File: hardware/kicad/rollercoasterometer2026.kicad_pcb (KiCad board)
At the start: 2 copper layers, 48.3 x 114.3 mm, 32 parts, among them J1 Micro_SD_Card, J102 Conn_02x07_Counter_Clockwise, J103 ZED-F9R U.FL, J104 LIS2MDL, J105 BMP595, J106 ADXL375, J4 SM03B-SRSS-TB, U101 RPiPico2, U102 ADIS16465-2BMLZ, U2 LIS2MDLTR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

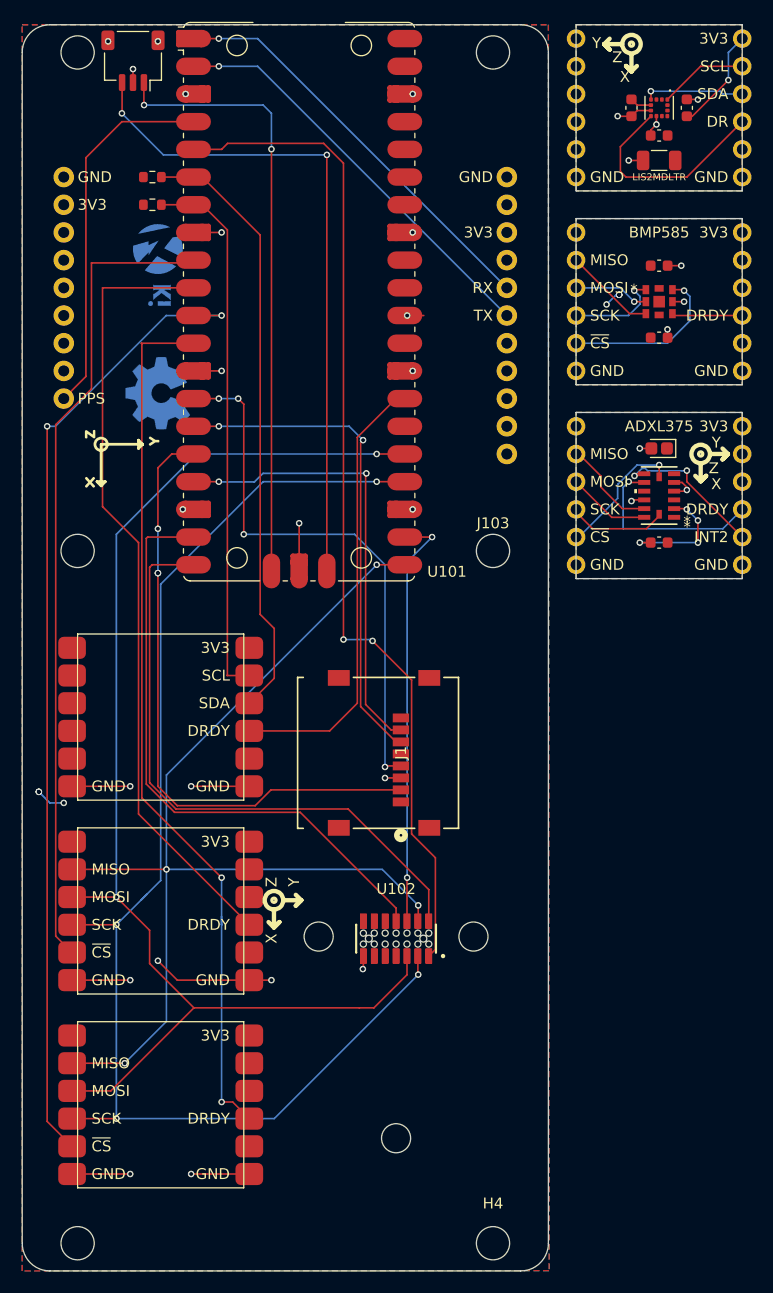
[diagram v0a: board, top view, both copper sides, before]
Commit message: Updated board to four layer design
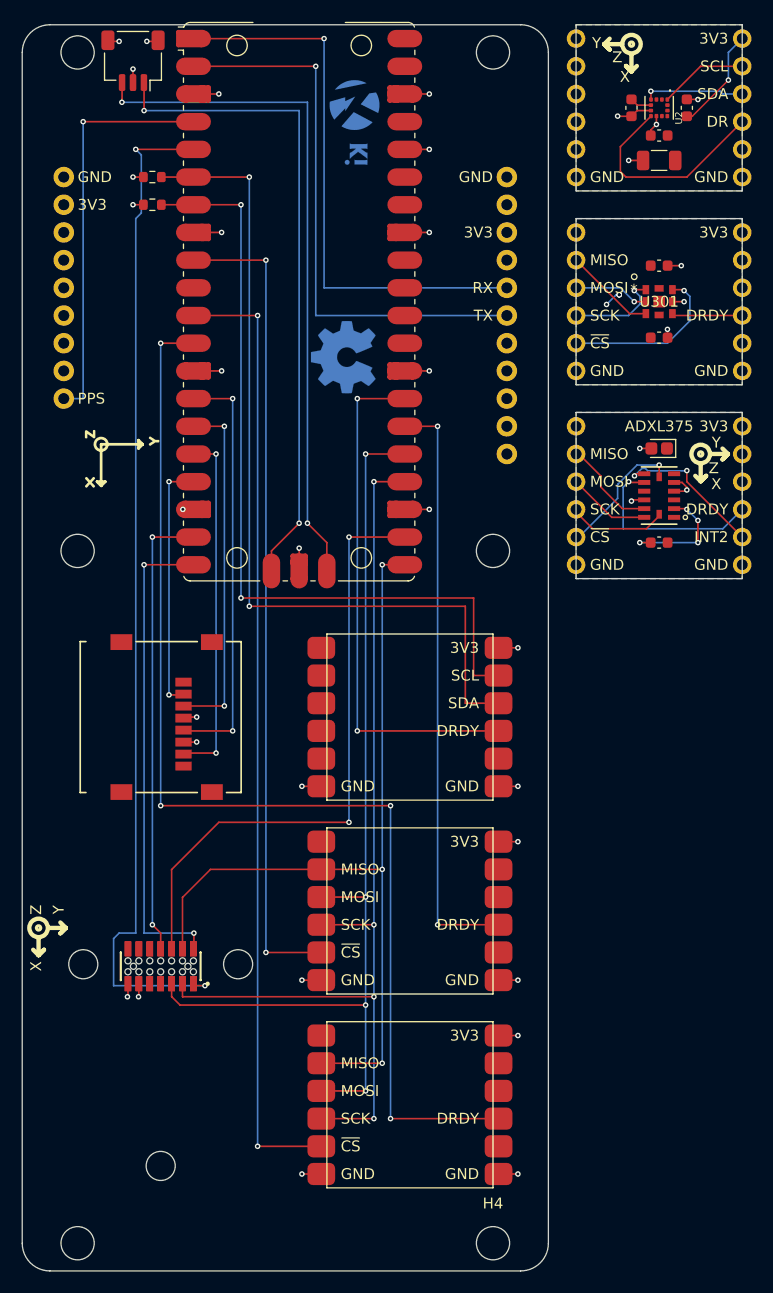
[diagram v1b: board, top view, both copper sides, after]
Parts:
- moved J104 22.9 mm to (109.2, 139.7)
- moved J105 22.9 mm to (109.2, 157.5)
- moved J106 22.9 mm to (109.2, 175.3)
- moved G103 22.4 mm to (104.1, 83.6)
- moved G102 22.2 mm to (104.4, 89.9)
- moved J102 21.7 mm to (86.4, 162.6)
- moved U102 21.7 mm to (86.4, 162.6)
- moved J101 20.2 mm to (86.4, 139.7)
- moved G101 17.3 mm to (103.1, 106.7)
- renumbered J1 to J101
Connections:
- U101 pad 10: /DR_BMP -> unconnected-(U101-GP7-Pad10)
- U101 pad 26: /~{CS}_MAG -> /DR_BMP
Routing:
- net /SCK0: track 119.9 -> 88.8 mm
- net /MOSI0: track 116.0 -> 88.6 mm, vias 2 -> 4
- net /MISO1: track 57.2 -> 31.7 mm, vias 3 -> 2
- net /SCL0: track 49.9 -> 74.1 mm, vias 0 -> 2
- net /DR_HIG: track 82.2 -> 105.9 mm, vias 2 -> 4
- net /SDA0: track 55.7 -> 79.2 mm, vias 0 -> 2
- net GND: track 58.7 -> 38.5 mm, vias 21 -> 20
- net /MISO0: track 96.5 -> 76.7 mm, vias 4 -> 3
- net /DR_BMP: track 73.1 -> 55.1 mm, vias 0 -> 2
- net /~{CS}_SD: track 41.0 -> 24.0 mm
- net /~{CS}_IMU: track 39.5 -> 55.8 mm
- net /~{RST}_IMU: track 56.5 -> 42.7 mm, vias 0 -> 2
- net /MOSI1: track 44.8 -> 31.4 mm
- net /TX_GPS: track 37.4 -> 50.8 mm
- net /RX_GPS: track 37.4 -> 50.8 mm
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- added copper zone on In2.Cu, net +3V3
- added copper zone on In1.Cu, net GND
- removed copper zone on F.Cu, net +3V3
- removed copper zone on B.Cu, net GND
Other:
- copper layers 2 -> 4
- rule pad_to_mask_clearance: 0.051 -> 0

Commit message: Moved sensors from stamp to direct placement
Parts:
- removed J104: LIS2MDL, footprints:StampPad
- removed J105: BMP595, footprints:StampPad
- removed J106: ADXL375, footprints:StampPad
- removed J201, J301, J401: ~, footprints:Stamp
- moved G302 63.4 mm to (113.3, 174.8)
- moved C406 60.6 mm to (109.2, 171.2)
- moved C208 60.4 mm to (109.2, 144.5)
- moved C209 60.4 mm to (109.2, 142.2)
- moved C304 60.4 mm to (109.2, 160.8)
- moved G301 60.4 mm to (106.7, 133.9)
- moved C210 60.4 mm to (111.8, 139.7)
- moved C308 60.4 mm to (109.2, 154.2)
- moved U2 60.4 mm to (109.2, 139.7)
- moved U301 60.4 mm to (109.2, 157.5)
- moved U401 60.4 mm to (109.2, 175.3)
- moved C205 60.4 mm to (106.7, 139.7)
- moved C401 59.9 mm to (109.2, 179.1)
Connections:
- C205 pad 2: /Magnetic Sensor/GND -> GND
- C208 pad 1: /Magnetic Sensor/3V3 -> +3V3
- C208 pad 2: /Magnetic Sensor/GND -> GND
- C209 pad 1: /Magnetic Sensor/3V3 -> +3V3
- C209 pad 2: /Magnetic Sensor/GND -> GND
- C210 pad 1: /Magnetic Sensor/3V3 -> +3V3
- C210 pad 2: /Magnetic Sensor/GND -> GND
- C304 pad 1: /Pressure Sensor/3V3 -> +3V3
- C304 pad 2: /Pressure Sensor/GND -> GND
- C308 pad 1: /Pressure Sensor/3V3 -> +3V3
- C308 pad 2: /Pressure Sensor/GND -> GND
- C401 pad 1: /HiG Sensor/3V3 -> +3V3
- C401 pad 2: /HiG Sensor/GND -> GND
- C406 pad 1: /HiG Sensor/3V3 -> +3V3
- C406 pad 2: /HiG Sensor/GND -> GND
- U2 pad 1: /Magnetic Sensor/SCL -> /SCL0
- U2 pad 10: /Magnetic Sensor/3V3 -> +3V3
- U2 pad 3: /Magnetic Sensor/3V3 -> +3V3
- U2 pad 4: /Magnetic Sensor/SDA -> /SDA0
- U2 pad 6: /Magnetic Sensor/GND -> GND
- U2 pad 7: /Magnetic Sensor/DRDY -> /DR_MAG
- U2 pad 8: /Magnetic Sensor/GND -> GND
- U2 pad 9: /Magnetic Sensor/3V3 -> +3V3
- U301 pad 1: /Pressure Sensor/SCK -> /SCK0
- U301 pad 2: /Pressure Sensor/MOSI -> /MOSI0
- U301 pad 3: /Pressure Sensor/MISO -> /MISO0
- U301 pad 4: /Pressure Sensor/3V3 -> +3V3
- U301 pad 5: /Pressure Sensor/DRDY -> /DR_BMP
- U301 pad 6: /Pressure Sensor/GND -> GND
- U301 pad 7: /Pressure Sensor/~{CS} -> /~{CS}_BMP
- U301 pad 8: /Pressure Sensor/3V3 -> +3V3
- U401 pad 1: /HiG Sensor/3V3 -> +3V3
- U401 pad 11: /HiG Sensor/GND -> GND
- U401 pad 12: /HiG Sensor/MISO -> /MISO0
- U401 pad 13: /HiG Sensor/MOSI -> /MOSI0
- U401 pad 14: /HiG Sensor/SCK -> /SCK0
- U401 pad 2: /HiG Sensor/GND -> GND
- U401 pad 3: /HiG Sensor/3V3 -> +3V3
- U401 pad 4: /HiG Sensor/GND -> GND
- U401 pad 5: /HiG Sensor/GND -> GND
- U401 pad 6: /HiG Sensor/3V3 -> +3V3
- U401 pad 7: /HiG Sensor/~{CS} -> /~{CS}_HIG
- U401 pad 9: /HiG Sensor/DRDY -> /DR_HIG
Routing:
- net /Magnetic Sensor/DRDY: track 19.6 -> 0.00 mm
- net /HiG Sensor/DRDY: track 17.5 -> 0.00 mm, vias 1 -> 0
- net /HiG Sensor/GND: track 16.1 -> 0.00 mm, vias 7 -> 0
- net /Pressure Sensor/~{CS}: track 15.0 -> 0.00 mm, vias 1 -> 0
- net +3V3: track 12.7 -> 27.1 mm, vias 8 -> 13
- net /HiG Sensor/INT2: track 14.2 -> 0.00 mm, vias 2 -> 0
- net /HiG Sensor/~{CS}: track 11.9 -> 0.00 mm, vias 1 -> 0
- net GND: track 38.5 -> 48.0 mm, vias 20 -> 25
- net /Magnetic Sensor/3V3: track 9.38 -> 0.00 mm, vias 1 -> 0
- net /HiG Sensor/SCK: track 8.99 -> 0.00 mm
- net /Magnetic Sensor/SDA: track 8.88 -> 0.00 mm, vias 1 -> 0
- net /HiG Sensor/MISO: track 8.61 -> 0.00 mm
- net /Pressure Sensor/SCK: track 8.48 -> 0.00 mm, vias 1 -> 0
- net /SDA0: track 79.2 -> 70.8 mm
- net /Pressure Sensor/MISO: track 8.28 -> 0.00 mm
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- removed copper zone on F.Cu, net /HiG Sensor/3V3
- removed copper zone on B.Cu, net /HiG Sensor/GND
- removed copper zone on F.Cu, net /Magnetic Sensor/3V3
- removed copper zone on B.Cu, net /Magnetic Sensor/GND
- removed copper zone on F.Cu, net /Pressure Sensor/3V3
- removed copper zone on B.Cu, net /Pressure Sensor/GND
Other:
- outline, holes or cut-outs redrawn

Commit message: Import rp2354 module
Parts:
- added C102: 10u, Capacitor_SMD:C_0805_2012Metric, F.Cu at (78.2, 87.4)
- added C103: 10u, Capacitor_SMD:C_0805_2012Metric, F.Cu at (89.4, 87.4)
- added C500: 10u, Capacitor_SMD:C_0805_2012Metric, F.Cu at (111.8, 188.0)
- added C501: 100n, Capacitor_SMD:C_0402_1005Metric, F.Cu at (77.3, 103.3)
- added C506: 100n, Capacitor_SMD:C_0402_1005Metric, F.Cu at (77.3, 105.7)
- added C511: 100n, Capacitor_SMD:C_0402_1005Metric, F.Cu at (77.3, 108.1)
- added C520: 100n, Capacitor_SMD:C_0402_1005Metric, F.Cu at (82.0, 112.8)
- added C521: 15p, Capacitor_SMD:C_0402_1005Metric, F.Cu at (82.4, 115.7)
- added C522: 15p, Capacitor_SMD:C_0402_1005Metric, F.Cu at (85.4, 115.7)
- added C523: 4.7u, Capacitor_SMD:C_0402_1005Metric, F.Cu at (84.6, 113.6)
- added C530: 100n, Capacitor_SMD:C_0402_1005Metric, F.Cu at (89.5, 110.7)
- added C538: 100n, Capacitor_SMD:C_0402_1005Metric, F.Cu at (90.9, 107.1)
- added C539: 100n, Capacitor_SMD:C_0402_1005Metric, F.Cu at (90.9, 106.1)
- added C544: 100n, Capacitor_SMD:C_0402_1005Metric, F.Cu at (90.3, 103.7)
- added C546: 4.7u, Capacitor_SMD:C_0402_1005Metric, F.Cu at (88.0, 101.6)
- added C549: 4.7u, footprints:C_0402_1005Metric_small_pads, F.Cu at (85.8, 102.1)
- added C550: 4.7u, footprints:C_0402_1005Metric_small_pads, F.Cu at (85.8, 101.1)
- added C553: 100n, Capacitor_SMD:C_0402_1005Metric, F.Cu at (81.7, 99.3)
- added H101: MountingHole, MountingHole:MountingHole_2.7mm_M2.5, F.Cu at (76.2, 78.7)
- added H102: MountingHole, MountingHole:MountingHole_2.7mm_M2.5, F.Cu at (119.9, 78.7)
- added J104: 2169900001, footprints:MOLEX_2169900001, F.Cu at (94.0, 76.2)
- added L550: 3.3u, footprints:L_pol_2016, F.Cu at (85.8, 99.5)
- added R101: 5.1k, Resistor_SMD:R_0402_1005Metric, F.Cu at (95.5, 85.9)
- added R102: 5.1k, Resistor_SMD:R_0402_1005Metric, F.Cu at (92.5, 85.9)
- added R522: 1k, Resistor_SMD:R_0402_1005Metric, F.Cu at (83.4, 113.6)
- added R526: 1k, Resistor_SMD:R_0402_1005Metric, F.Cu at (254.3, 89.4)
- added R546: 33, Resistor_SMD:R_0402_1005Metric, F.Cu at (88.0, 99.8)
- added R551: 27, Resistor_SMD:R_0402_1005Metric, F.Cu at (83.7, 99.3)
- added R552: 27, Resistor_SMD:R_0402_1005Metric, F.Cu at (82.7, 99.3)
- added R560: 1k, Resistor_SMD:R_0402_1005Metric, F.Cu at (77.2, 100.8)
- added S526: SW_Push, Button_Switch_SMD:SW_SPST_B3U-1000P, F.Cu at (68.8, 114.4)
- added S560: SW_Push, Button_Switch_SMD:SW_Push_1P1T_NO_Vertical_Wuerth_434133025816, F.Cu at (68.6, 121.6)
- added U501: RP2354A, footprints:RP2350-QFN-60-1EP_7x7_P0.4mm_EP3.4x3.4mm_ThermalVias, F.Cu at (83.8, 106.7)
- added Y501: ABM8-272-T3, Crystal:Crystal_SMD_3225-4Pin_3.2x2.5mm, F.Cu at (83.8, 119.1)
- R106, R107: footprint Resistor_SMD:R_0603_1608Metric -> Resistor_SMD:R_0402_1005Metric
- U101: value RPiPico2 -> NCP1117-3.3_SOT223; footprint footprints:RaspberryPi_Pico_Original_SMD -> Package_TO_SOT_SMD:SOT-223-3_TabPin2
- moved J103 57.2 mm to (119.4, 69.8)
- moved R106 52.6 mm to (109.2, 137.2), turned to 180 degrees
- moved R107 49.2 mm to (109.2, 135.9)
- moved G102 42.4 mm to (62.7, 98.0)
- moved G101 40.4 mm to (62.7, 108.5)
- moved G103 22.7 mm to (126.7, 85.1)
- moved U101 19.8 mm to (83.8, 88.9), turned to 180 degrees
- moved J101 9.77 mm to (82.3, 130.8)
- moved H103 2.54 mm to (76.2, 188.0)
- moved H104 2.54 mm to (119.4, 188.0)
- renumbered H3 to H103, H4 to H104, J4 to J105
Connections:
- U101 pad 1: /RX_GPS -> GND
- U101 pad 2: /TX_GPS -> +3V3
- U101 pad 3: GND -> VBUS
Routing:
- net /DR_HIG: track 108.2 -> 0.00 mm, vias 4 -> 0
- net /DR_IMU: track 94.5 -> 0.00 mm, vias 2 -> 0
- net /~{CS}_HIG: track 89.3 -> 0.00 mm, vias 2 -> 0
- net /MOSI0: track 89.4 -> 2.41 mm, vias 4 -> 1
- net /SCK0: track 86.3 -> 5.06 mm, vias 4 -> 1
- net /~{CS}_BMP: track 78.9 -> 0.00 mm, vias 2 -> 0
- net /MISO0: track 78.7 -> 7.08 mm, vias 4 -> 1
- net /SDA0: track 70.8 -> 0.00 mm, vias 2 -> 0
- net /SCL0: track 69.8 -> 0.00 mm, vias 2 -> 0
- net /SWD: track 61.5 -> 3.55 mm, vias 2 -> 1
- net /SWCLK: track 59.3 -> 1.85 mm, vias 2 -> 1
- net /TX_GPS: track 50.8 -> 0.00 mm, vias 1 -> 0
- net /RX_GPS: track 50.8 -> 0.00 mm, vias 1 -> 0
- net /DR_BMP: track 50.6 -> 1.69 mm, vias 2 -> 1
- net /~{CS}_IMU: track 55.8 -> 7.22 mm, vias 2 -> 1
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- added copper zone on F.Cu, net +3V3
- added copper zone on F.Cu, net /Controller/1V1
- added copper zone on F.Cu, net /Controller/VREG_LX
- added copper zone on F.Cu, net GND
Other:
- outline, holes or cut-outs redrawn
